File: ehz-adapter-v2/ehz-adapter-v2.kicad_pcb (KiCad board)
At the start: 2 copper layers, 32 x 32 mm, 19 parts, among them J3 Conn_01x02_Male, Q1 SFH 309 FA-5/6, Q2 BSS138, U1 mh-et-live-minikit, U2 D-SUN-MP1584EN, U3 LMV7235M7X

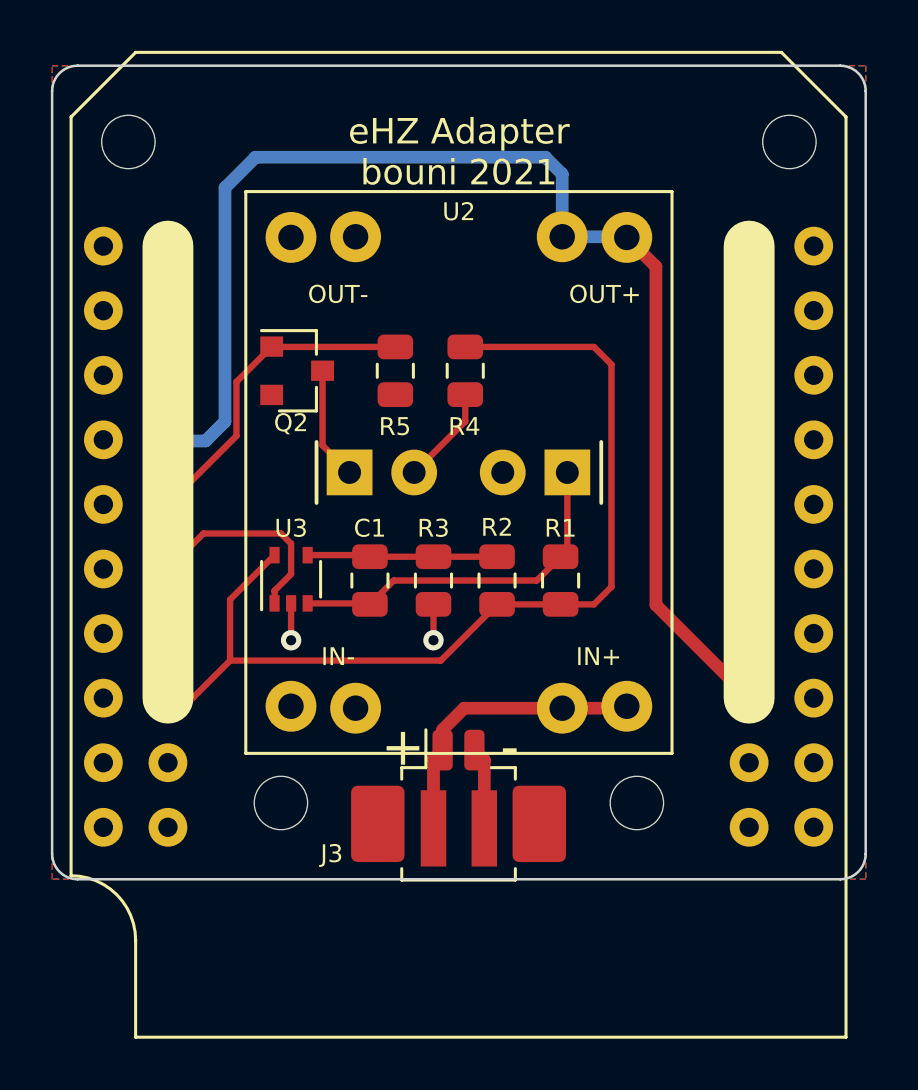
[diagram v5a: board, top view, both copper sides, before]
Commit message: Replaced D-SUN with custom Buck converter
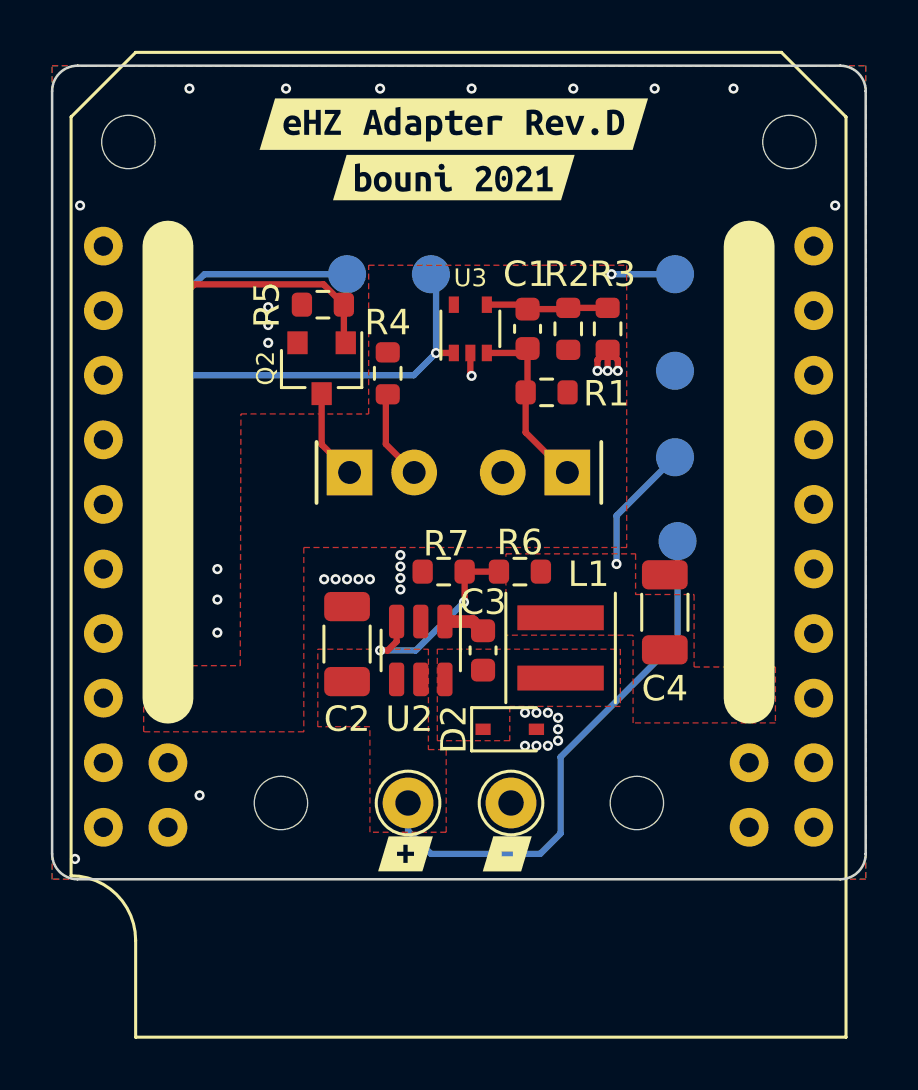
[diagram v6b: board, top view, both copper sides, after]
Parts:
- removed J3: Conn_01x02_Male, Connector_Molex:Molex_PicoBlade_53261-0271_1x02-1MP_P1.25mm_Horizontal
- added C2: 2.2uF, Capacitor_SMD:C_1206_3216Metric, F.Cu at (50.6, 61.8)
- added C3: 100nF, Capacitor_SMD:C_0603_1608Metric, F.Cu at (56.0, 62.0)
- added C4: 10uF, Capacitor_SMD:C_1206_3216Metric, F.Cu at (63.1, 60.5)
- added D2: 1N5819WS, Diode_SMD:D_SOD-323, F.Cu at (57.0, 65.1)
- added J1: Conn_01x01_Female, Connector_Pin:Pin_D1.0mm_L10.0mm, F.Cu at (53.0, 68.0)
- added J2: Conn_01x01_Female, Connector_Pin:Pin_D1.0mm_L10.0mm, F.Cu at (57.0, 68.0)
- added L1: 10uH, Inductor_SMD:L_Coilcraft_XxL4020, F.Cu at (59.0, 61.9)
- added R6: 54.9k, Resistor_SMD:R_0603_1608Metric, F.Cu at (57.4, 58.9)
- added R7: 10k, Resistor_SMD:R_0603_1608Metric, F.Cu at (54.4, 58.9)
- added TP3: TestPoint, TestPoint:TestPoint_Pad_D1.5mm, B.Cu at (63.5, 54.4)
- added TP4: TestPoint, TestPoint:TestPoint_Pad_D1.5mm, B.Cu at (63.5, 47.2)
- added TP5: TestPoint, TestPoint:TestPoint_Pad_D1.5mm, B.Cu at (53.9, 47.2)
- added TP6: TestPoint, TestPoint:TestPoint_Pad_D1.5mm, B.Cu at (50.6, 47.2)
- added kibuzzard-61B75BD6: G***, kibuzzard-61B75BD6, F.Cu at (54.8, 41.3)
- added kibuzzard-61B75BED: G***, kibuzzard-61B75BED, F.Cu at (54.8, 43.4)
- added kibuzzard-61B75BFD: G***, kibuzzard-61B75BFD, F.Cu at (52.9, 70.0)
- added kibuzzard-61B75C18: G***, kibuzzard-61B75C18, F.Cu at (56.9, 70.0)
- C1: footprint Capacitor_SMD:C_0805_2012Metric -> Capacitor_SMD:C_0603_1608Metric
- R1, R2, R3, R5: footprint Resistor_SMD:R_0805_2012Metric -> Resistor_SMD:R_0603_1608Metric
- R4: value 100R -> 100; footprint Resistor_SMD:R_0805_2012Metric -> Resistor_SMD:R_0603_1608Metric
- TP1, TP2: footprint bouni:SolderPad1x3 -> TestPoint:TestPoint_Pad_D1.5mm; moved to B.Cu
- U2: value D-SUN-MP1584EN -> LMR16006YQ; footprint Bouni:D-SUN-MP1584EN -> Package_TO_SOT_SMD:SOT-23-6
- moved TP2 19.5 mm to (63.5, 51.0)
- moved TP1 14.8 mm to (63.6, 57.7)
- moved U3 12.1 mm to (55.5, 49.4)
- moved R3 12.0 mm to (60.9, 49.4)
- moved C1 11.7 mm to (57.7, 49.4)
- moved R2 10.3 mm to (59.3, 49.4)
- moved R1 7.42 mm to (58.5, 51.9), turned to 180 degrees
- moved U2 7.16 mm to (53.5, 62.0), turned to -90 degrees
- moved R5 3.86 mm to (49.6, 48.4), turned to 180 degrees
- moved R4 3.05 mm to (52.2, 51.1)
- moved Q2 0.97 mm to (49.6, 50.9), turned to -90 degrees
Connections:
- TP1 pad 1: Net-(J3-Pad1) -> /vin
- U1 pad 10: (no net) -> unconnected-(U1-Pad10)
- U1 pad 11: (no net) -> unconnected-(U1-Pad11)
- U1 pad 12: (no net) -> BLINK
- U1 pad 13: (no net) -> RX
- U1 pad 14: (no net) -> unconnected-(U1-Pad14)
- U1 pad 15: BLINK -> unconnected-(U1-Pad15)
- U1 pad 16: RX -> unconnected-(U1-Pad16)
- U1 pad 17: (no net) -> unconnected-(U1-Pad17)
- U1 pad 19: (no net) -> unconnected-(U1-Pad19)
- U1 pad 2: (no net) -> unconnected-(U1-Pad2)
- U1 pad 20: (no net) -> unconnected-(U1-Pad20)
- U1 pad 21: (no net) -> unconnected-(U1-Pad21)
- U1 pad 22: (no net) -> unconnected-(U1-Pad22)
- U1 pad 23: (no net) -> unconnected-(U1-Pad23)
- U1 pad 24: (no net) -> unconnected-(U1-Pad24)
- U1 pad 25: (no net) -> unconnected-(U1-Pad25)
- U1 pad 26: (no net) -> unconnected-(U1-Pad26)
- U1 pad 29: (no net) -> unconnected-(U1-Pad29)
- U1 pad 3: (no net) -> unconnected-(U1-Pad3)
- U1 pad 30: (no net) -> unconnected-(U1-Pad30)
- U1 pad 32: (no net) -> unconnected-(U1-Pad32)
- U1 pad 33: (no net) -> unconnected-(U1-Pad33)
- U1 pad 34: (no net) -> unconnected-(U1-Pad34)
- U1 pad 35: (no net) -> unconnected-(U1-Pad35)
- U1 pad 36: (no net) -> unconnected-(U1-Pad36)
- U1 pad 37: (no net) -> unconnected-(U1-Pad37)
- U1 pad 38: (no net) -> unconnected-(U1-Pad38)
- U1 pad 39: (no net) -> unconnected-(U1-Pad39)
- U1 pad 4: (no net) -> unconnected-(U1-Pad4)
- U1 pad 40: (no net) -> unconnected-(U1-Pad40)
- U1 pad 5: (no net) -> unconnected-(U1-Pad5)
- U1 pad 6: (no net) -> unconnected-(U1-Pad6)
- U1 pad 7: (no net) -> unconnected-(U1-Pad7)
- U1 pad 8: (no net) -> unconnected-(U1-Pad8)
- U1 pad 9: (no net) -> unconnected-(U1-Pad9)
- U2 pad 1: GND -> Net-(C3-Pad1)
- U2 pad 3: Net-(J3-Pad1) -> Net-(R6-Pad2)
- U2 pad 4: Net-(J3-Pad1) -> unconnected-(U2-Pad4)
- U2 pad 5: GND -> /vin
- U2 pad 6: GND -> /sw
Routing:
- net +5V: track 50.9 -> 5.15 mm, vias 0 -> 1
- net +3V3: track 38.9 -> 2.50 mm, vias 0 -> 1
- net /vin: track 0.00 -> 21.2 mm
- net Net-(J3-Pad1): track 12.5 -> 0.00 mm
- net Net-(R6-Pad2): track 0.00 -> 8.23 mm, vias 0 -> 2
- net Net-(C1-Pad1): track 14.2 -> 7.30 mm
- net RX: track 8.21 -> 14.8 mm, vias 0 -> 1
- net BLINK: track 12.8 -> 16.8 mm
- net Net-(C1-Pad2): track 7.48 -> 4.84 mm
- net GND: track 5.35 -> 3.73 mm, vias 2 -> 39
- net Net-(C3-Pad1): track 0.00 -> 1.60 mm
- net Net-(D1-Pad1): track 4.44 -> 3.56 mm
- added copper zone on F.Cu, net +3V3
- added copper zone on F.Cu, net +5V
- added copper zone on F.Cu, net /sw
- added copper zone on F.Cu, net /vin
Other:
- board text added: "3.3V"
- board text added: "5V"
- board text added: "BLINK"
- board text added: "GND"
- board text added: "RX"
- board text added: "VIN"
- board text removed: "eHZ Adapter bouni 2021"

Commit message: added custom buck converter
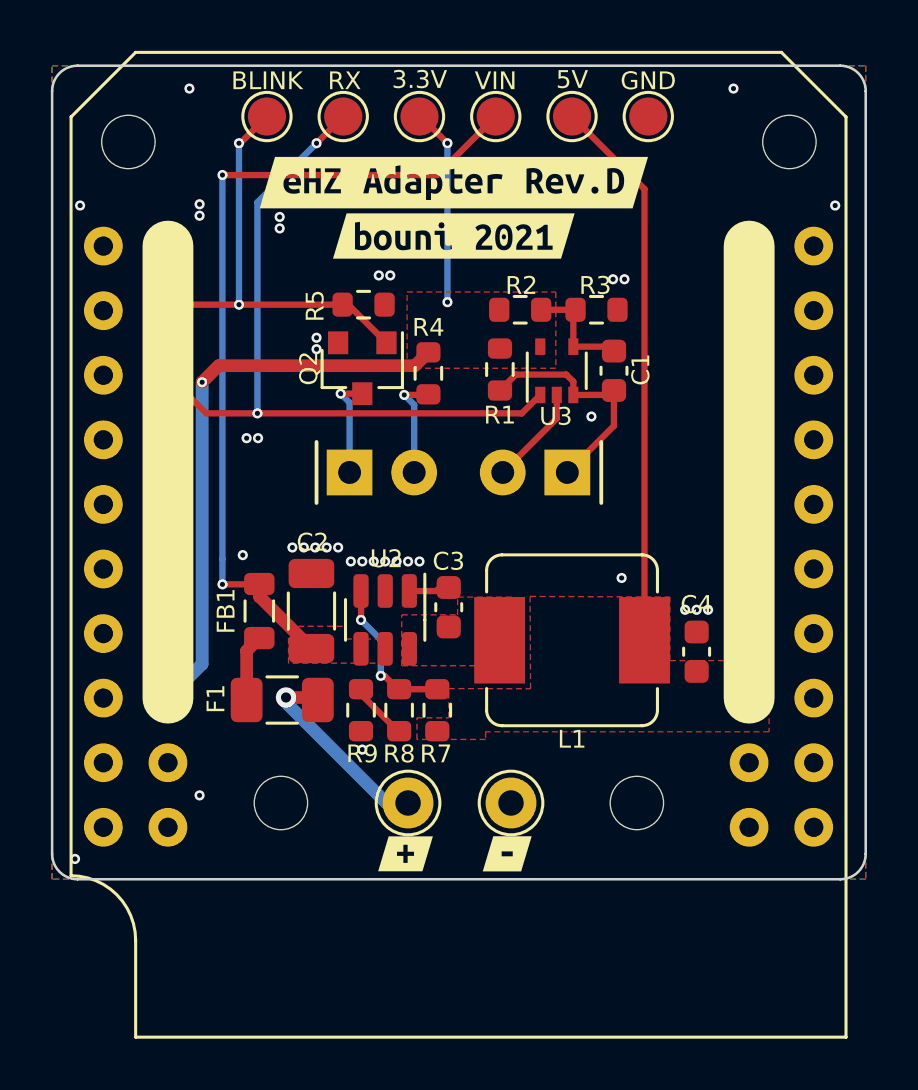
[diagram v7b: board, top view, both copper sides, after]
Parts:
- removed D2: 1N5819WS, Diode_SMD:D_SOD-323
- removed R6: 54.9k, Resistor_SMD:R_0603_1608Metric
- added F1: 1A, Fuse:Fuse_1206_3216Metric, F.Cu at (48.0, 64.0)
- added FB1: 600 @ 600MHz, Inductor_SMD:L_0805_2012Metric, F.Cu at (47.1, 60.5)
- added R8: 18k, Resistor_SMD:R_0603_1608Metric, F.Cu at (52.6, 64.3)
- added R9: 750, Resistor_SMD:R_0603_1608Metric, F.Cu at (51.1, 64.3)
- C2: value 2.2uF -> 2.2u
- C3: value 100nF -> 10n
- C4: value 10uF -> 10u; footprint Capacitor_SMD:C_1206_3216Metric -> Capacitor_SMD:C_0603_1608Metric
- L1: value 10uH -> 15uH; footprint Inductor_SMD:L_Coilcraft_XxL4020 -> Inductor_SMD:L_Sumida_CDMC6D28_7.25x6.5mm
- Q2: value BSS138 -> AO3400A
- R7: value 10k -> 100k
- TP1, TP2, TP3, TP4, TP5, TP6: moved to F.Cu
- U2: value LMR16006YQ -> LMR54410
- moved TP1 16.7 mm to (62.5, 41.0), turned to 90 degrees
- moved TP3 14.0 mm to (59.5, 41.0), turned to 90 degrees
- moved TP2 12.2 mm to (56.5, 41.0), turned to 90 degrees
- moved TP4 11.8 mm to (53.5, 41.0), turned to 90 degrees
- moved TP5 7.10 mm to (50.5, 41.0)
- moved TP6 6.95 mm to (47.5, 41.0)
- moved R7 5.46 mm to (54.1, 64.3), turned to 90 degrees
- moved C1 3.78 mm to (61.1, 51.0)
- moved U3 3.78 mm to (58.9, 51.0)
- moved kibuzzard-61B75BD6 2.30 mm to (54.8, 43.6)
- moved kibuzzard-61B75BED 2.30 mm to (54.8, 45.7)
- moved C3 2.17 mm to (54.6, 60.3), turned to 90 degrees
- moved R1 2.05 mm to (56.6, 51.0), turned to -90 degrees
- moved R2 2.03 mm to (57.4, 48.6), turned to 0 degrees
- moved C4 1.99 mm to (64.3, 62.0)
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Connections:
- C2 pad 1: /vin -> /VIN
- C3 pad 1: Net-(C3-Pad1) -> /SW
- C3 pad 2: /sw -> /CB
- J1 pad 1: /vin -> /24V
- L1 pad 1: /sw -> /SW
- R7 pad 1: Net-(R6-Pad2) -> +5V
- R7 pad 2: GND -> /FB
- TP1 pad 1: /vin -> GND
- TP2 pad 1: GND -> /VIN
- U2 pad 1: Net-(C3-Pad1) -> /CB
- U2 pad 3: Net-(R6-Pad2) -> /FB
- U2 pad 4: unconnected-(U2-Pad4) -> /VIN
- U2 pad 5: /vin -> /VIN
- U2 pad 6: /sw -> /SW
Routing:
- net /VIN: track 0.00 -> 32.6 mm, vias 0 -> 2
- net +3V3: track 2.50 -> 30.1 mm, vias 1 -> 3
- net /vin: track 21.2 -> 0.00 mm
- net +5V: track 5.15 -> 21.8 mm, vias 1 -> 0
- net RX: track 14.8 -> 28.6 mm, vias 1 -> 2
- net Net-(R6-Pad2): track 8.23 -> 0.00 mm, vias 2 -> 0
- net /24V: track 0.00 -> 8.04 mm, vias 0 -> 1
- net /FB: track 0.00 -> 5.91 mm, vias 0 -> 2
- net Net-(F1-Pad1): track 0.00 -> 2.64 mm
- net Net-(C1-Pad1): track 7.30 -> 9.65 mm
- net Net-(R8-Pad2): track 0.00 -> 2.21 mm
- net Net-(C3-Pad1): track 1.60 -> 0.00 mm
- net /CB: track 0.00 -> 1.26 mm
- net Net-(C1-Pad2): track 4.84 -> 4.26 mm
- net Net-(D1-Pad2): track 3.61 -> 4.17 mm, vias 0 -> 1
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- added copper zone on F.Cu, net /SW
- added copper zone on F.Cu, net /VIN
- removed copper zone on F.Cu, net /sw
- removed copper zone on F.Cu, net /vin
